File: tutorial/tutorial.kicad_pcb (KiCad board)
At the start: 2 copper layers, 36.8 x 15.2 mm, 5 parts, among them J1 MYCONN3, U1 PIC12C508A-I/SN

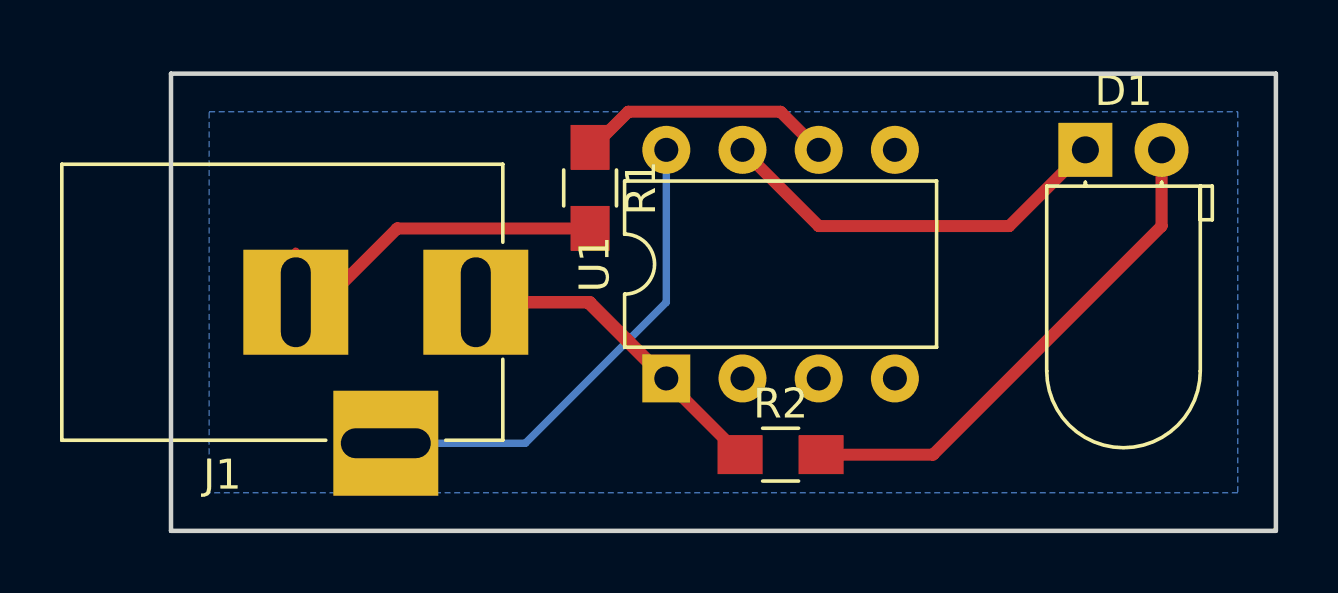
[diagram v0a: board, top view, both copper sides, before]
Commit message: Changed to microUSB connector
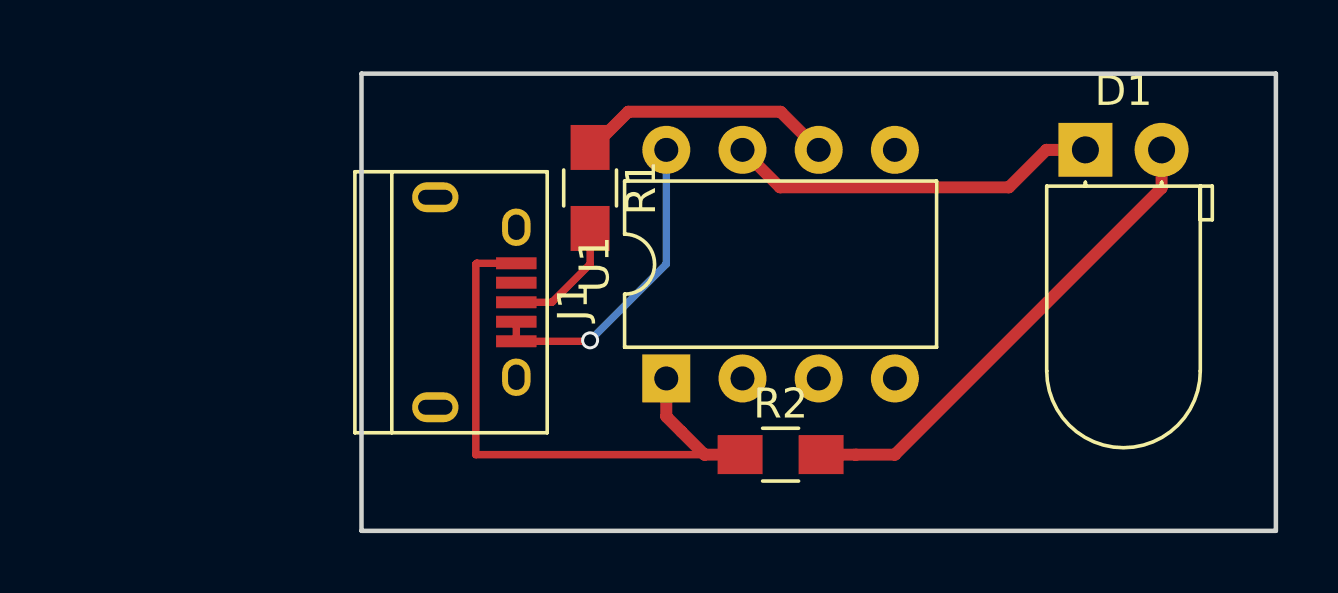
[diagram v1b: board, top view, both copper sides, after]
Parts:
- J1: value MYCONN3 -> USB_B; footprint Connectors:BARREL_JACK -> Connectors:USB_Micro-B
- turned J1 to 270 degrees
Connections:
- J1 pad 3: GND -> Net-(J1-Pad3)
- R1 pad 2: Net-(J1-Pad2) -> Net-(J1-Pad3)
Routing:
- net Net-(J1-Pad2): track 12.9 -> 0.00 mm
- net GND: track 16.4 -> 10.5 mm, vias 0 -> 1
- net Net-(J1-Pad3): track 0.00 -> 4.18 mm
- net VCC: track 18.3 -> 20.8 mm
- net /uCtoLED: track 13.5 -> 12.5 mm
- net Net-(D1-Pad2): track 17.0 -> 16.3 mm
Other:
- board size 36.8 x 15.2 mm -> 30.5 x 15.2 mm
